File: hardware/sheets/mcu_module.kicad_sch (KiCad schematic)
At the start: 0 parts

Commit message: hw: draw MCU module and debug sheets (#6)
* hw: draw MCU module and debug sheets

Draw the MDBT53-P1M with Raytac's normal-voltage DC/DC reference
circuit (Ver.E section 8.1.2): VDD and VDDH on 3V3 with 4.7 uF, a
10 uH inductor and 1 uF on each internal regulator output, and module
VBUS through 2.2 ohm with 4.7 uF. The 32.768 kHz crystal uses the
nRF5340's internal 9 pF load, with external load caps left unfitted.
USB D+/D- reach the module through 0 ohm links that can take the
27 ohm resistors shown in Raytac's figure.

The debug sheet has the ARM Cortex 10-pin SWD header and pads for
reset, SWD, UART, ground and six spare GPIO. The header connects to
the nRF5340 DK's debug out; pin 3 is grounded so the DK selects the
external target.

Labels whose other end belongs on a sheet not drawn yet are excluded
from ERC with a comment naming that sheet, to be removed as each
sheet is drawn.

* docs: describe the module supply and debug setup

Record the module's reference-circuit parts, the 0 ohm USB data links
and the SWD header in the hardware overview. State the DC/DC inductor
limits as TDK specifies them: 90 mA maximum for at most a 50%
inductance drop, with 250 mA only a typical temperature-rise
reference, against Nordic's reference BOM.

Debugging uses the nRF5340 DK's debug out. Nordic requires the target
voltage to match the DK, which runs at 3 V on USB alone, so bring-up
supplies the DK's nRF5340 with 3.3 V on its external input and checks
that the two voltages match before connecting. Bring-up also checks
the module's DC/DC regulators.

* ci: avoid SIGPIPE when printing host tool versions

Under pipefail, `--version | head -n 1` can fail the host-dependency
script when head exits before the tool finishes writing. Capture the
whole version output and print its first line instead.
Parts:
- added C401, C402: 4.7uF 16V, Capacitor_SMD:C_0603_1608Metric, symbol Device:C
- added C403, C404: 1uF, Capacitor_SMD:C_0402_1005Metric, symbol Device:C
- added C405, C406: DNP, Capacitor_SMD:C_0402_1005Metric, symbol Device:C
- added L401, L402: 10uH, Inductor_SMD:L_0603_1608Metric, symbol Device:L
- added R401: 2.2, Resistor_SMD:R_0603_1608Metric, symbol Device:R
- added R402, R403: 0, Resistor_SMD:R_0402_1005Metric, symbol Device:R
- added U401: MDBT53-P1M, smart-led-badge:Raytac_MDBT53-P1M, symbol smart-led-badge:MDBT53-P1M
- added Y401: 32.768kHz 9pF, Crystal:Crystal_SMD_3215-2Pin_3.2x1.5mm, symbol Device:Crystal
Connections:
- new net +3V3: C401.1, U401.38 (VDD), U401.41 (VDDH)
- new net BTN_ACTION: U401.53 (P1.12)
- new net BTN_MODE: U401.55 (P1.11)
- new net CC1_SENSE: U401.39 (P0.05/AIN1)
- new net CC2_SENSE: U401.35 (P0.06/AIN2)
- new net CHG_CE: U401.65 (P0.29)
- new net CHG_INT: U401.57 (P0.30)
- new net CHG_STAT: U401.49 (P1.14)
- new net DCC: L401.1, U401.54 (DCC)
- new net DCCD: L402.1, U401.50 (DCCD)
- new net DECD: C404.1, L402.2, U401.52 (DECD)
- new net DECR: C403.1, L401.2, U401.58 (DECR)
- new net GND: C401.2, C402.2, C403.2, C404.2, C405.2, C406.2, U401.1 (GND), U401.24 (GND), U401.42 (GND), U401.61 (GND)
- new net I2C1_SCL: U401.33 (P1.02/TWI)
- new net I2C1_SDA: U401.31 (P1.03/TWI)
- new net IMU_CS_FB: U401.56 (P0.31)
- new net IMU_INT1: U401.11 (P1.04)
- new net IMU_INT2: U401.22 (P1.05)
- new net IMU_SDO_FB: U401.3 (P1.08)
- new net LED_EN: U401.13 (P0.20)
- new net MTX_ARM: U401.14 (P0.19)
- new net MTX_BLANK: U401.15 (P0.12/HSPI_DCX)
- new net MTX_LAT: U401.17 (P0.11/HSPI_CSN)
- new net MTX_MISO: U401.18 (P0.10/HSPI_MISO)
- new net MTX_MOSI: U401.19 (P0.09/HSPI_MOSI)
- new net MTX_SAFE_SENSE: U401.12 (P0.21)
- new net MTX_SCK: U401.29 (P0.08/HSPI_SCK)
- new net NFC_FD: U401.10 (P1.06)
- new net NFC_PWR: U401.59 (P1.10)
- new net NFC_SCL: U401.43 (P1.01)
- new net NFC_SDA: U401.45 (P1.00)
- new net PDM_CLK: U401.63 (P1.07)
- new net PDM_DIN: U401.64 (P1.09)
- new net PWR_SW_N: U401.47 (P1.15)
- new net SPARE_P0_02: U401.32 (P0.02/NFC1)
- new net SPARE_P0_03: U401.30 (P0.03/NFC2)
- new net SPARE_P0_13: U401.21 (P0.13/QSPI0)
- new net SPARE_P0_14: U401.27 (P0.14/QSPI1)
- new net SPARE_P0_26: U401.7 (P0.26/AIN5)
- new net SPARE_P0_27: U401.5 (P0.27/AIN6)
- new net STATUS_LED: U401.51 (P1.13)
- new net SWDCLK: U401.2 (SWDCLK)
- new net SWDIO: U401.4 (SWDIO)
- new net UART_RX: U401.62 (P0.23)
- new net UART_TX: U401.25 (P0.22)
- new net USB_DN: R403.1
- new net USB_DN_MOD: R403.2, U401.48 (D-)
- new net USB_DP: R402.1
- new net USB_DP_MOD: R402.2, U401.46 (D+)
- new net VBAT_MEAS_EN: U401.8 (P0.24)
- new net VBAT_SENSE: U401.37 (P0.04/AIN0)
- new net VBUS: R401.1
- new net VBUS_MOD: C402.1, R401.2, U401.44 (VBUS)
- new net VLED_SENSE: U401.9 (P0.25/AIN4)
- new net XL1: C405.1, U401.34 (P0.00/XL1), Y401.1
- new net XL2: C406.1, U401.36 (P0.01/XL2), Y401.2
- new net nRESET: U401.6 (nRESET)
- no-connect marks 0 -> 7
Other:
- note added: "MCU module (Rev A) - design notes Raytac MDBT53-P1M (nRF5340, PCB antenna), Ver.E 2024-10-25, reference circuit 8.1.2 (normal voltage, DC/DC): VDD = VDDH = 3V3 with 4.7 uF (C401); DCCH not connected; DCC-L401-DECR and DCCD-L402-DECD with 1 uF each. Module VBUS (pin 44) through 2.2 ohm (R401) with 4.7 uF (C402); the charger branch does not pass through R401. USB D+/D- via 0 ohm links R402/R403 fro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"

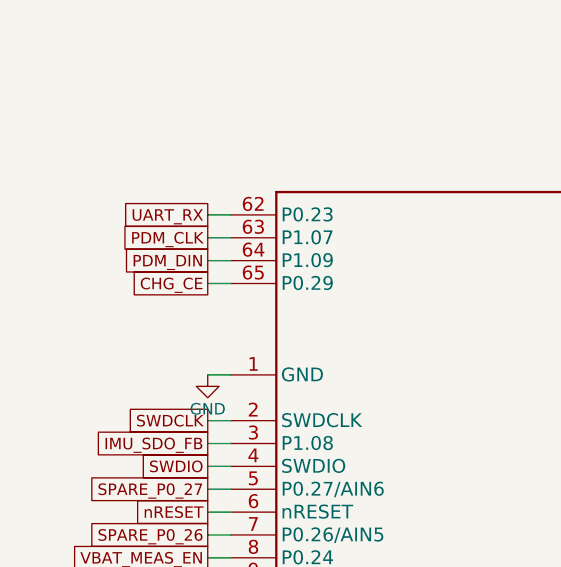
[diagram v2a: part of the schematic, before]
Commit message: hw: freeze the Rev A schematic for layout (#12)
* hw: freeze the Rev A schematic for layout

The freeze review checked every sheet against the netlist and the parts'
datasheets: rails and enables, charger and regulator capacitors, matrix
start-up and blanking, test points, USB, I2C, PDM, fault states and
back-power paths. No circuit change was needed.

The sheets' title blocks and the hardware documents now mark the
schematic as frozen for layout. Later changes go through a recorded
decision; the matrix LED footprint still follows the final LED part.
Points for bring-up include the VBUS attach capacitance, the charger
enable while 3V3 is absent, VLED loop stability and VBUS-before-VDD
behaviour.

* hw: hold the charger CE high unless the MCU enables charging

CE was pulled up to 3V3, so with USB present and the logic rail absent
(the first milliseconds after attach, or a failed 3V3 rail) it went low
and the charger charged at its reset settings, whose cold limit can be
as low as -1.5 C.

R313 now pulls CE up to SYS, which is present whenever the battery or
USB is (CE is rated to 6 V). Q303 (AO3400A) pulls CE low only while
P0.29 drives the new CHG_EN net high, and R316 holds CHG_EN low
otherwise. Charging therefore stays off in MCU reset, with the MCU
unpowered or with 3V3 missing, not only at start-up.

* fw: drive the charger enable as active-high CHG_EN

P0.29 now drives the gate of Q303 instead of the charger's CE pin, so
the board's zephyr,user property becomes chg-en-gpios, active high:
asserted means charging is allowed.

* docs: record the freeze conclusions for charging, USB and battery sensing

Charging: the CE hardware now keeps charging off without the MCU, and
the charger's reset temperature limits are never relied on.

Battery sensing: the switch, divider, leakage, ADC configuration,
settling, error budget and proposed shed margin are recorded with final
values. SAADC accuracy relies on per-board calibration.

USB: the VBUS attach capacitance (15.7 uF 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
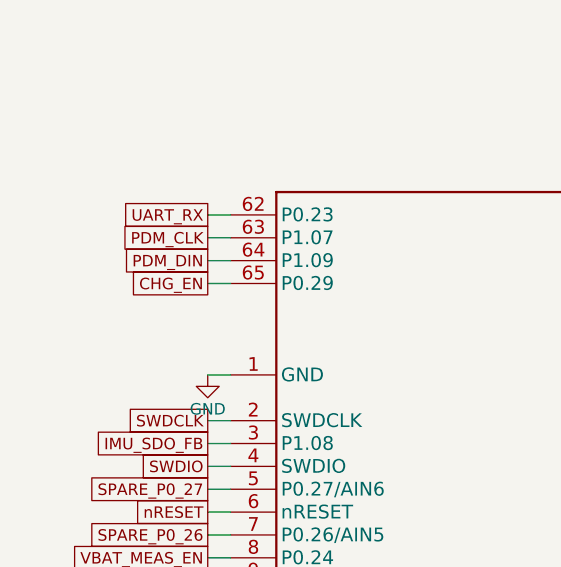
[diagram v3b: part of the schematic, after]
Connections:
- net CHG_CE renamed CHG_EN
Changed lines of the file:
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@@
 	(title_block
 		(title "MCU Module")
+		(date "2026-10-07")
 		(rev "A")
 		(comment 1 "Smart LED Badge Rev A")
-		(comment 2 "Draft: schematic capture in progress, not for fabrication")
+		(comment 2 "Schematic frozen for layout after review 2026-10-07; not for fabrication until the release gate")
 	)
 	(text "MCU module (Rev A) - design notes\n\nRaytac MDBT53-P1M (nRF5340, PCB antenna), Ver.E 2024-10-25, reference circuit 8.1.2 (normal voltage, DC/DC):\nVDD = VDDH = 3V3 with 4.7 uF (C401); DCCH not connected; DCC-L401-DECR and DCCD-L402-DECD with 1 uF each.\nModule VBUS (pin 44) through 2.2 ohm (R401) with 4.7 uF (C402); the charger branch does not pass through R401.\nUSB D+/D- via 0 ohm links R402/R403 from the TPD4E05U06 (charger sheet); 27 ohm footprint option per Raytac figure.\nLFXO: CM7V-T1A 9 pF on XL1/XL2 (P0.00/P0.01) with the nRF5340 internal 9 pF load; C405/C406 DNP.\nNFC1/NFC2 pins used as spare GPIO (CONFIG_NFCT_PINS_AS_GPIOS); native NFC unused.\nSpare GPIO P0.02/03/13/14/26/27 go to debug-sheet pads; P0.07/15/16/17/18/28 unconnected.\nAntenna: keep the Raytac keep-out (all layers) clear of copper, battery, magnets and screws.\nPin map: IMPLEMENTATION DECISION, verified against the project symbol (Ver.E 2.5). Nothing measured."
@@
 		)
 	)
-	(global_label "CHG_CE"
+	(global_label "CHG_EN"
 		(shape passive)
 		(at 109.22 73.66 180)
